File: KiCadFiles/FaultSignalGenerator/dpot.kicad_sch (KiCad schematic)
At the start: 4 parts

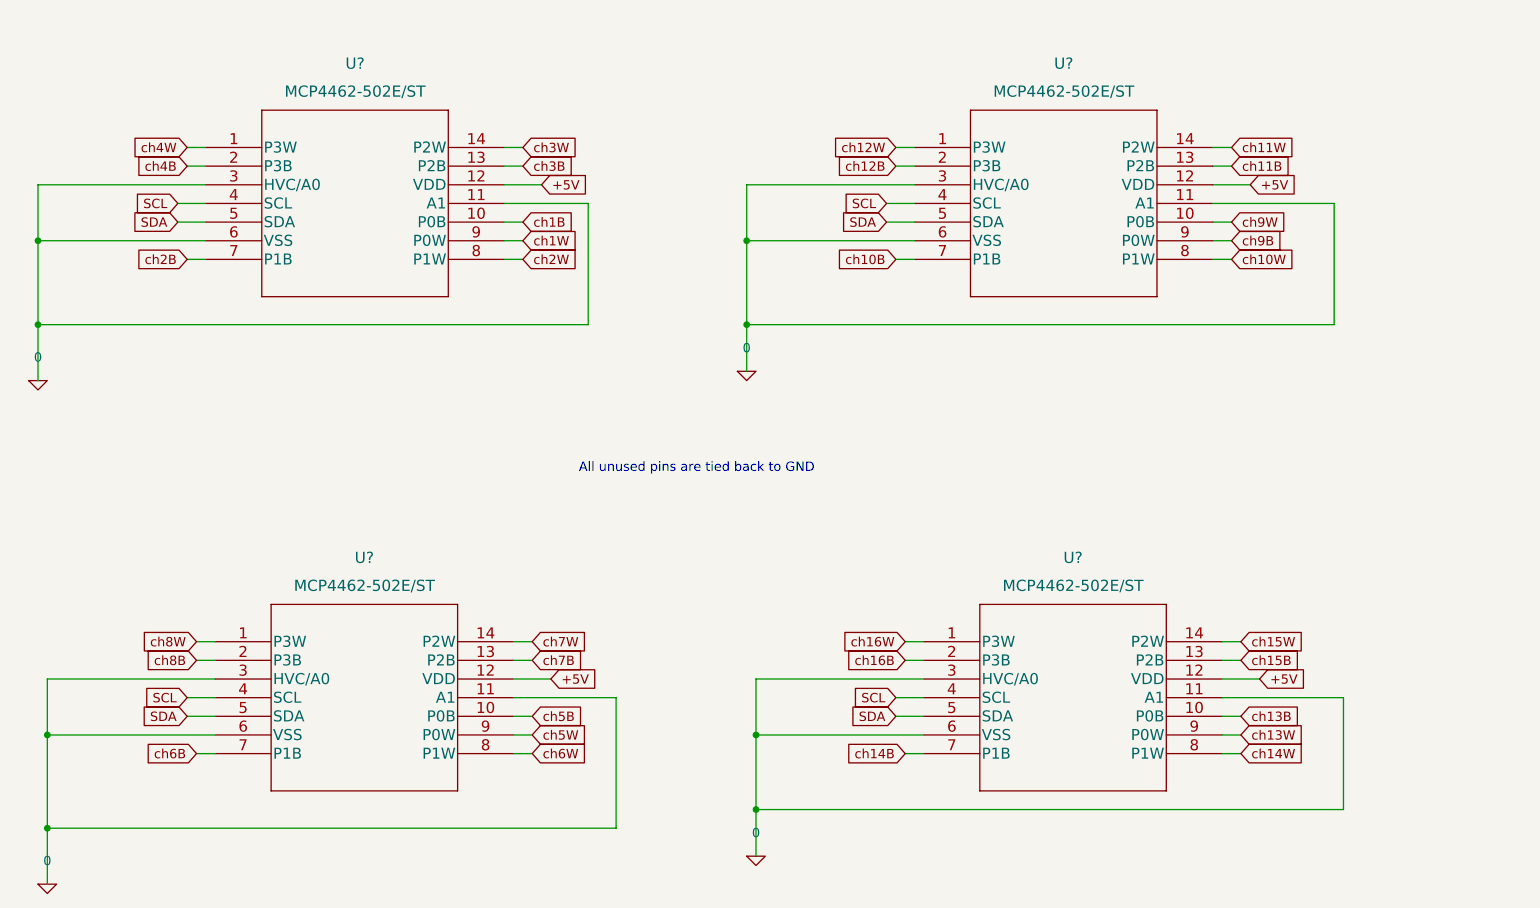
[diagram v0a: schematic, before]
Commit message: Finish schematic, start on PCB
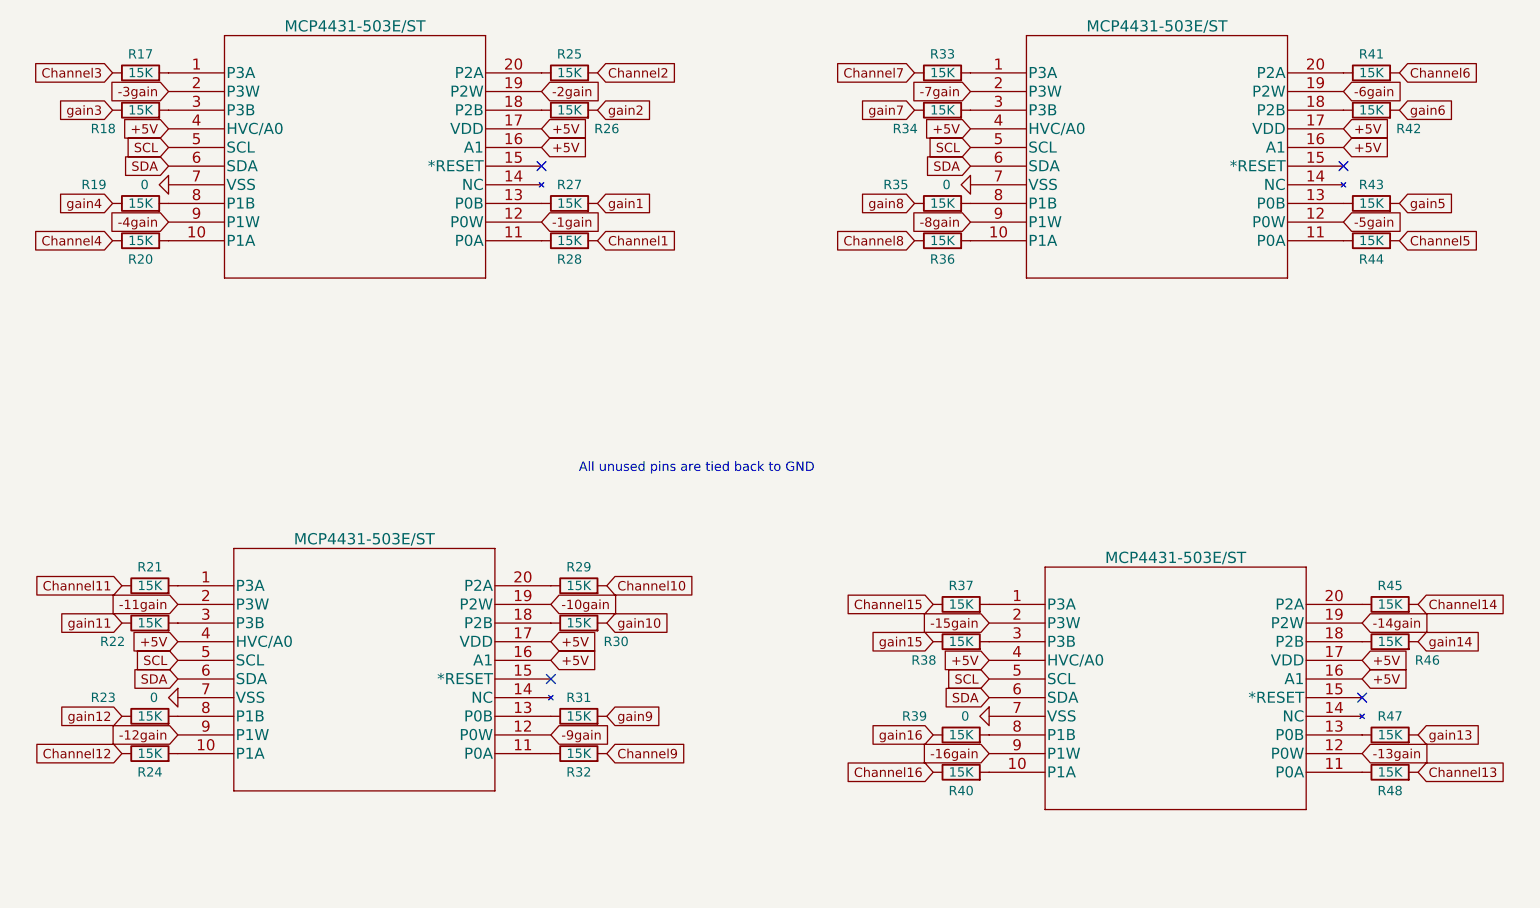
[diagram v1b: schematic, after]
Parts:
- removed U? (x4): MCP4462-502E/ST, DPOT:MCP4462-502E&slash_ST, symbol 2023-01-31_02-59-41:MCP4462-502E/ST
- added R17, R18, R19, R20, R21, R22, R23, R24, R25, R26, R27, R28, R29, R30, R31, R32, R33, R34, R35, R36, R37, R38, R39, R40, R41, R42, R43, R44, R45, R46, R47, R48: 15K, Resistor_SMD:R_1206_3216Metric, symbol Device:R
- added U1, U2, U3, U4: MCP4431-503E/ST, Package_SO:TSSOP-20_4.4x6.5mm_P0.65mm, symbol FaultSignalGeneratorCustomSymbols:MCP4431-503E/ST
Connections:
- net +5V: now also U1.16 (A1), U1.17 (VDD), U1.4 (HVC/A0), U2.16 (A1), U2.17 (VDD), U2.4 (HVC/A0), U3.16 (A1), U3.17 (VDD), U3.4 (HVC/A0), U4.16 (A1), U4.17 (VDD), U4.4 (HVC/A0)
- net 0: now also U1.7 (VSS), U2.7 (VSS), U3.7 (VSS), U4.7 (VSS)
- net SCL: now also U1.5 (SCL), U2.5 (SCL), U3.5 (SCL), U4.5 (SCL)
- net SDA: now also U1.6 (SDA), U2.6 (SDA), U3.6 (SDA), U4.6 (SDA)
- new net: R23.2, U2.8 (P1B)
- new net: R40.2, U4.10 (P1A)
- new net: R42.1, U3.18 (P2B)
- new net: R37.2, U4.1 (P3A)
- new net: R48.1, U4.11 (P0A)
- new net: R47.1, U4.13 (P0B)
- new net: R46.1, U4.18 (P2B)
- new net: R45.1, U4.20 (P2A)
- new net: R38.2, U4.3 (P3B)
- new net: R39.2, U4.8 (P1B)
- new net: R18.2, U1.3 (P3B)
- new net: R20.2, U1.10 (P1A)
- new net: R26.1, U1.18 (P2B)
- new net: R17.2, U1.1 (P3A)
- new net: R28.1, U1.11 (P0A)
- new net: R27.1, U1.13 (P0B)
- new net: R25.1, U1.20 (P2A)
- new net: R19.2, U1.8 (P1B)
- new net: R41.1, U3.20 (P2A)
- new net: R32.1, U2.11 (P0A)
- new net: R35.2, U3.8 (P1B)
- new net: R36.2, U3.10 (P1A)
- new net: R33.2, U3.1 (P3A)
- new net: R44.1, U3.11 (P0A)
- new net: R43.1, U3.13 (P0B)
- new net: R34.2, U3.3 (P3B)
- new net: R29.1, U2.20 (P2A)
- new net: R24.2, U2.10 (P1A)
- new net: R21.2, U2.1 (P3A)
- new net: R31.1, U2.13 (P0B)
- new net: R30.1, U2.18 (P2B)
- new net: R22.2, U2.3 (P3B)
- new net -10gain: U2.19 (P2W)
- new net -11gain: U2.2 (P3W)
- new net -12gain: U2.9 (P1W)
- new net -13gain: U4.12 (P0W)
- new net -14gain: U4.19 (P2W)
- new net -15gain: U4.2 (P3W)
- new net -16gain: U4.9 (P1W)
- new net -1gain: U1.12 (P0W)
- new net -2gain: U1.19 (P2W)
- new net -3gain: U1.2 (P3W)
- new net -4gain: U1.9 (P1W)
- new net -5gain: U3.12 (P0W)
- new net -6gain: U3.19 (P2W)
- new net -7gain: U3.2 (P3W)
- new net -8gain: U3.9 (P1W)
- new net -9gain: U2.12 (P0W)
- new net Channel1: R28.2
- new net Channel10: R29.2
- new net Channel11: R21.1
- new net Channel12: R24.1
- new net Channel13: R48.2
- new net Channel14: R45.2
- new net Channel15: R37.1
- new net Channel16: R40.1
- new net Channel2: R25.2
- new net Channel3: R17.1
- new net Channel4: R20.1
- new net Channel5: R44.2
- new net Channel6: R41.2
- new net Channel7: R33.1
- new net Channel8: R36.1
- new net Channel9: R32.2
- new net gain1: R27.2
- new net gain10: R30.2
- new net gain11: R22.1
- new net gain12: R23.1
- new net gain13: R47.2
- new net gain14: R46.2
- new net gain15: R38.1
- new net gain16: R39.1
- new net gain2: R26.2
- new net gain3: R18.1
- new net gain4: R19.1
- new net gain5: R43.2
- new net gain6: R42.2
- new net gain7: R34.1
- new net gain8: R35.1
- new net gain9: R31.2
- no-connect marks 0 -> 4
